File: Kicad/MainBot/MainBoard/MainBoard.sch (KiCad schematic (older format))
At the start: 20 parts, among them U1 AZ1117-3.3, U2 Teensy3.6

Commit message: update
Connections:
- net SCL1: now reaches U2.34 (37_A18_PWM_SCL1)
- net SDA1: now reaches U2.35 (38_A19_PWM_SDA1)
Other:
- note added: "Teensy/Raspeberry Pi \n comm channel\n"
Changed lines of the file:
@@
 Wire Wire Line
 	4700 4250 3900 4250
+Text Notes 750  6800 0    60   ~ 0
+Teensy/Raspeberry Pi \n    comm channel\n
+Wire Wire Line
+	4700 5050 4600 5050
+Wire Wire Line
+	4700 5150 4600 5150
+Text Label 4650 5050 2    60   ~ 0
+SCL1
+Text Label 4650 5150 2    60   ~ 0
+SDA1
 $EndSCHEMATC

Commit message: Ajout Comm Série Rasp/Teensy
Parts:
- added J?: Conn_01x02, symbol Conn_01x02
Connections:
- net RX1: now reaches J?.23 (Pin_23), U2.2 (0_RX1_MOSI1_Touch)
- net TX1: now reaches J?.22 (Pin_22), U2.3 (1_TX1_MISO1_Touch)
- new net RX_1: J?.2 (Pin_2)
- new net TX_1: J?.1 (Pin_1)
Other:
- note added: "-> RX_Pi\n-> TX_Pi"
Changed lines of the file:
@@
 Wire Wire Line
 	4700 4250 3900 4250
-Text Notes 750  6800 0    60   ~ 0
+Text Notes 500  7400 0    60   ~ 0
 Teensy/Raspeberry Pi \n    comm channel\n
 Wire Wire Line
@@
 Text Label 4650 5150 2    60   ~ 0
 SDA1
+Text Label 4150 1950 0    60   ~ 0
+TX1
+Text Label 4200 1850 0    60   ~ 0
+RX1
+$Comp
+L Conn_01x02 J?
+U 1 1 5C5C40DB
+P 1000 7550
+F 0 "J?" H 1000 7650 50  0000 C CNN
+F 1 "Conn_01x02" H 1000 7350 50  0000 C CNN
+F 2 "" H 1000 7550 50  0001 C CNN
+F 3 "" H 1000 7550 50  0001 C CNN
+	1    1000 7550
+	1    0    0    -1
+$EndComp
+Text Notes 1050 7700 0    60   ~ 0
+-> RX_Pi\n-> TX_Pi
+Wire Wire Line
+	800  7550 750  7550
+Wire Wire Line
+	800  7650 750  7650
+Text Label 750  7550 2    60   ~ 0
+TX_1
+Text Label 750  7650 2    60   ~ 0
+RX_1
 $EndSCHEMATC

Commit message: Added I2C pull-up resistor, I2C multiplexer
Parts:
- added R? (x2): R, symbol R
- added U?: TCA9548A, symbol TCA9548A
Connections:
- net GND: now also U?.~ (Vin)
- net SCL1: now also R?.1, U?.~ (Vin)
- net SDA1: now also R?.1, U?.~ (Vin)
- net VCC: now also R?.2, R?.2, U?.~ (Vin)
- net PWM17: now reaches U2.32 (35_A16_PWM)
- net PWM16: now reaches U2.33 (36_A17_PWM)
- no-connect marks 20 -> 21
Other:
- note added: "I2C Pull-up\nresistors\n"
- note added: "I2C multiplexer\n\n"
- note added: "Teensy/Raspberry Pi \n comm channel\n"
- note removed: "Teensy/Raspeberry Pi \n comm channel\n"
- moved on the sheet: J?
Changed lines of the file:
@@
 	1    0    0    -1
 $EndComp
-Wire Wire Line
-	1100 1500 1000 1500
-Wire Wire Line
-	1700 1500 1800 1500
-Wire Wire Line
-	6700 2950 6850 2950
 $Comp
 L GND #PWR?
@@
 	1    0    0    -1
 $EndComp
-Wire Wire Line
-	10300 1150 10650 1150
-Wire Wire Line
-	10300 1350 10500 1350
-Wire Wire Line
-	10500 1450 10300 1450
-Wire Wire Line
-	10300 1550 10500 1550
-Wire Wire Line
-	10500 1650 10300 1650
 NoConn ~ 10300 1750
 NoConn ~ 9350 1150
@@
 	0    -1   -1   0
 $EndComp
-Wire Wire Line
-	9350 1550 9300 1550
-Wire Wire Line
-	9350 1650 9300 1650
-Wire Wire Line
-	9350 1750 9300 1750
-Wire Wire Line
-	9350 1850 9300 1850
 Text Label 9300 1550 2    60   ~ 0
 STEP_RST_1
@@
 	0    -1   -1   0
 $EndComp
-Connection ~ 10500 1150
 $Comp
 L +12V #PWR?
@@
 NoConn ~ 9350 2550
 NoConn ~ 9350 2450
-Wire Wire Line
-	10300 2450 10500 2450
 $Comp
 L +12V #PWR?
@@
 $EndComp
 NoConn ~ 10300 3050
-Wire Wire Line
-	10300 2650 10500 2650
-Wire Wire Line
-	10500 2750 10300 2750
-Wire Wire Line
-	10300 2850 10500 2850
-Wire Wire Line
-	10500 2950 10300 2950
-Wire Wire Line
-	10300 3750 10500 3750
 $Comp
 L C C?
@@
 	1    0    0    -1
 $EndComp
-Wire Wire Line
-	10300 3950 10500 3950
-Wire Wire Line
-	10500 4050 10300 4050
-Wire Wire Line
-	10300 4150 10500 4150
-Wire Wire Line
-	10500 4250 10300 4250
 NoConn ~ 10300 4350
 $Comp
@@
 	1    0    0    -1
 $EndComp
-Wire Wire Line
-	10300 5050 10500 5050
 $Comp
 L C C?
@@
 	1    0    0    -1
 $EndComp
-Wire Wire Line
-	10300 5250 10500 5250
-Wire Wire Line
-	10500 5350 10300 5350
-Wire Wire Line
-	10300 5450 10500 5450
-Wire Wire Line
-	10500 5550 10300 5550
 NoConn ~ 10300 5650
 $Comp
@@
 Text Label 10750 6250 2    60   ~ 0
 DC_PWM_4
-Wire Wire Line
-	3900 2850 4700 2850
-Wire Wire Line
-	3900 2750 4700 2750
-Wire Wire Line
-	3900 2650 4700 2650
-Wire Wire Line
-	3900 2550 4700 2550
-Wire Wire Line
-	3900 2450 4700 2450
-Wire Wire Line
-	3900 2350 4700 2350
-Wire Wire Line
-	3900 2250 4700 2250
-Wire Wire Line
-	3900 2150 4700 2150
-Wire Wire Line
-	3900 3850 4700 3850
-Wire Wire Line
-	6700 5350 6750 5350
-Wire Wire Line
-	6700 5450 6800 5450
-Wire Wire Line
-	6700 5550 6850 5550
-Wire Wire Line
-	6700 5650 6900 5650
-Wire Wire Line
-	3900 3750 4700 3750
 $Comp
 L GND #PWR?
@@
 	0    -1   -1   0
 $EndComp
-Wire Wire Line
-	4700 1850 3900 1850
-Wire Wire Line
-	3900 1950 4700 1950
-Wire Wire Line
-	4700 2050 3900 2050
-Wire Wire Line
-	4700 2950 3900 2950
-Wire Wire Line
-	4700 3050 3900 3050
-Wire Wire Line
-	3900 3150 4700 3150
-Wire Wire Line
-	4700 3250 3900 3250
-Wire Wire Line
-	3900 3350 4700 3350
-Wire Wire Line
-	4700 3450 3900 3450
-Wire Wire Line
-	4700 3550 3900 3550
-Wire Wire Line
-	4700 3650 3900 3650
-Wire Wire Line
-	3900 3950 4700 3950
-Wire Wire Line
-	4700 4050 3900 4050
 $Comp
 L GND #PWR?
@@
 	-1   0    0    1
 $EndComp
-Wire Wire Line
-	3900 4150 4700 4150
-Wire Wire Line
-	4700 4250 3900 4250
-Text Notes 500  7400 0    60   ~ 0
-Teensy/Raspeberry Pi \n    comm channel\n
-Wire Wire Line
-	4700 5050 4600 5050
-Wire Wire Line
-	4700 5150 4600 5150
-Text Label 4650 5050 2    60   ~ 0
+Text Notes 500  7350 0    60   ~ 0
+Teensy/Raspberry Pi \n    comm channel\n
+Text Label 4350 5050 2    60   ~ 0
 SCL1
-Text Label 4650 5150 2    60   ~ 0
+Text Label 4450 5150 2    60   ~ 0
 SDA1
 Text Label 4150 1950 0    60   ~ 0
@@
 L Conn_01x02 J?
 U 1 1 5C5C40DB
-P 1000 7550
-F 0 "J?" H 1000 7650 50  0000 C CNN
-F 1 "Conn_01x02" H 1000 7350 50  0000 C CNN
-F 2 "" H 1000 7550 50  0001 C CNN
-F 3 "" H 1000 7550 50  0001 C CNN
-	1    1000 7550
-	1    0    0    -1
-$EndComp
-Text Notes 1050 7700 0    60   ~ 0
+P 1000 7500
+F 0 "J?" H 1000 7600 50  0000 C CNN
+F 1 "Conn_01x02" H 1000 7300 50  0000 C CNN
+F 2 "" H 1000 7500 50  0001 C CNN
+F 3 "" H 1000 7500 50  0001 C CNN
+	1    1000 7500
+	1    0    0    -1
+$EndComp
+Text Notes 1050 7650 0    60   ~ 0
 -> RX_Pi\n-> TX_Pi
-Wire Wire Line
-	800  7550 750  7550
-Wire Wire Line
-	800  7650 750  7650
-Text Label 750  7550 2    60   ~ 0
+Text Label 750  7500 2    60   ~ 0
 TX_1
-Text Label 750  7650 2    60   ~ 0
+Text Label 750  7600 2    60   ~ 0
 RX_1
+Text Notes 2200 6500 0    60   ~ 0
+I2C multiplexer\n\n
+$Comp
+L TCA9548A U?
+U 1 1 5C5C5BB5
+P 2700 7100
+F 0 "U?" H 2500 7750 60  0000 C CNN
+F 1 "TCA9548A" H 2700 6450 60  0000 C CNN
+F 2 "" H 2600 7150 60  0001 C CNN
+F 3 "" H 2600 7150 60  0001 C CNN
+	1    2700 7100
+	1    0    0    -1
+$EndComp
+$Comp
+L VCC #PWR?
+U 1 1 5C5C69D4
+P 2250 6550
+F 0 "#PWR?" H 2250 6400 50  0001 C CNN
+F 1 "VCC" H 2250 6700 50  0000 C CNN
+F 2 "" H 2250 6550 50  0001 C CNN
+F 3 "" H 2250 6550 50  0001 C CNN
+	1    2250 6550
+	0    -1   -1   0
+$EndComp
+$Comp
+L GND #PWR?
+U 1 1 5C5C6A14
+P 2000 6650
+F 0 "#PWR?" H 2000 6400 50  0001 C CNN
+F 1 "GND" H 2000 6500 50  0000 C CNN
+F 2 "" H 2000 6650 50  0001 C CNN
+F 3 "" H 2000 6650 50  0001 C CNN
+	1    2000 6650
+	0    1    1    0
+$EndComp
+Text Label 2200 6750 2    60   ~ 0
+SDA1
+Text Label 2200 6850 2    60   ~ 0
+SCL1
+$Comp
+L R R?
+U 1 1 5C5C7D15
+P 950 7050
+F 0 "R?" V 1030 7050 50  0000 C CNN
+F 1 "R" V 950 7050 50  0000 C CNN
+F 2 "" V 880 7050 50  0001 C CNN
+F 3 "" H 950 7050 50  0001 C CNN
+	1    950  7050
+	0    -1   -1   0
+$EndComp
+$Comp
+L R R?
+U 1 1 5C5C8548
+P 950 6850
+F 0 "R?" V 1030 6850 50  0000 C CNN
+F 1 "R" V 950 6850 50  0000 C CNN
+F 2 "" V 880 6850 50  0001 C CNN
+F 3 "" H 950 6850 50  0001 C CNN
+	1    950  6850
+	0    -1   -1   0
+$EndComp
+$Comp
+L VCC #PWR?
+U 1 1 5C5C8903
+P 1100 7050
+F 0 "#PWR?" H 1100 6900 50  0001 C CNN
+F 1 "VCC" H 1100 7200 50  0000 C CNN
+F 2 "" H 1100 7050 50  0001 C CNN
+F 3 "" H 1100 7050 50  0001 C CNN
+	1    1100 7050
+	0    1    1    0
+$EndComp
+$Comp
+L VCC #PWR?
+U 1 1 5C5C8947
+P 1100 6850
+F 0 "#PWR?" H 1100 6700 50  0001 C CNN
+F 1 "VCC" H 1100 7000 50  0000 C CNN
+F 2 "" H 1100 6850 50  0001 C CNN
+F 3 "" H 1100 6850 50  0001 C CNN
+	1    1100 6850
+	0    1    1    0
+$EndComp
+Text Label 750  7050 2    60   ~ 0
+SCL1
+Text Label 750  6850 2    60   ~ 0
+SDA1
+Text Notes 500  6750 0    60   ~ 0
+I2C Pull-up\nresistors\n
+NoConn ~ 2250 6950
+Text Label 4550 4950 2    60   ~ 0
+PWM16
+Text Label 4450 4850 2    60   ~ 0
+PWM17
+Wire Wire Line
+	1100 1500 1000 1500
+Wire Wire Line
+	1700 1500 1800 1500
+Wire Wire Line
+	6700 2950 6850 2950
+Wire Wire Line
+	10300 1150 10650 1150
+Wire Wire Line
+	10300 1350 10500 1350
+Wire Wire Line
+	10500 1450 10300 1450
+Wire Wire Line
+	10300 1550 10500 1550
+Wire Wire Line
+	10500 1650 10300 1650
+Wire Wire Line
+	9350 1550 9300 1550
+Wire Wire Line
+	9350 1650 9300 1650
+Wire Wire Line
+	9350 1750 9300 1750
+Wire Wire Line
+	9350 1850 9300 1850
+Connection ~ 10500 1150
+Wire Wire Line
+	10300 2450 10500 2450
+Wire Wire Line
+	10300 2650 10500 2650
+Wire Wire Line
+	10500 2750 10300 2750
+Wire Wire Line
+	10300 2850 10500 2850
+Wire Wire Line
+	10500 2950 10300 2950
+Wire Wire Line
+	10300 3750 10500 3750
+Wire Wire Line
+	10300 3950 10500 3950
+Wire Wire Line
+	10500 4050 10300 4050
+Wire Wire Line
+	10300 4150 10500 4150
+Wire Wire Line
+	10500 4250 10300 4250
+Wire Wire Line
+	10300 5050 10500 5050
+Wire Wire Line
+	10300 5250 10500 5250
+Wire Wire Line
+	10500 5350 10300 5350
+Wire Wire Line
+	10300 5450 10500 5450
+Wire Wire Line
+	10500 5550 10300 5550
+Wire Wire Line
+	3900 2850 4700 2850
+Wire Wire Line
+	3900 2750 4700 2750
+Wire Wire Line
+	3900 2650 4700 2650
+Wire Wire Line
+	3900 2550 4700 2550
+Wire Wire Line
+	3900 2450 4700 2450
+Wire Wire Line
+	3900 2350 4700 2350
+Wire Wire Line
+	3900 2250 4700 2250
+Wire Wire Line
+	3900 2150 4700 2150
+Wire Wire Line
+	3900 3850 4700 3850
+Wire Wire Line
+	6700 5350 6750 5350
+Wire Wire Line
+	6700 5450 6800 5450
+Wire Wire Line
+	6700 5550 6850 5550
+Wire Wire Line
+	6700 5650 6900 5650
+Wire Wire Line
+	3900 3750 4700 3750
+Wire Wire Line
+	4700 1850 3900 1850
+Wire Wire Line
+	3900 1950 4700 1950
+Wire Wire Line
+	4700 2050 3900 2050
+Wire Wire Line
+	4700 2950 3900 2950
+Wire Wire Line
+	4700 3050 3900 3050
+Wire Wire Line
+	3900 3150 4700 3150
+Wire Wire Line
+	4700 3250 3900 3250
+Wire Wire Line
+	3900 3350 4700 3350
+Wire Wire Line
+	4700 3450 3900 3450
+Wire Wire Line
+	4700 3550 3900 3550
+Wire Wire Line
+	4700 3650 3900 3650
+Wire Wire Line
+	3900 3950 4700 3950
+Wire Wire Line
+	4700 4050 3900 4050
+Wire Wire Line
+	3900 4150 4700 4150
+Wire Wire Line
+	4700 4250 3900 4250
+Wire Wire Line
+	4350 5050 4700 5050
+Wire Wire Line
+	4450 5150 4700 5150
+Wire Wire Line
+	800  7500 750  7500
+Wire Wire Line
+	800  7600 750  7600
+Wire Wire Line
+	2000 6650 2250 6650
+Wire Wire Line
+	2250 6750 2200 6750
+Wire Wire Line
+	2250 6850 2200 6850
+Wire Wire Line
+	800  7050 750  7050
+Wire Wire Line
+	750  6850 800  6850
+Wire Notes Line
+	500  7150 1500 7150
+Wire Notes Line
+	1300 7150 1300 6550
+Wire Notes Line
+	1300 6550 500  6550
+Wire Notes Line
+	500  6550 500  7750
+Wire Notes Line
+	500  7750 1500 7750
+Wire Notes Line
+	1500 7750 1500 7150
+Wire Wire Line
+	4700 4950 4550 4950
+Wire Wire Line
+	4700 4850 4450 4850
 $EndSCHEMATC

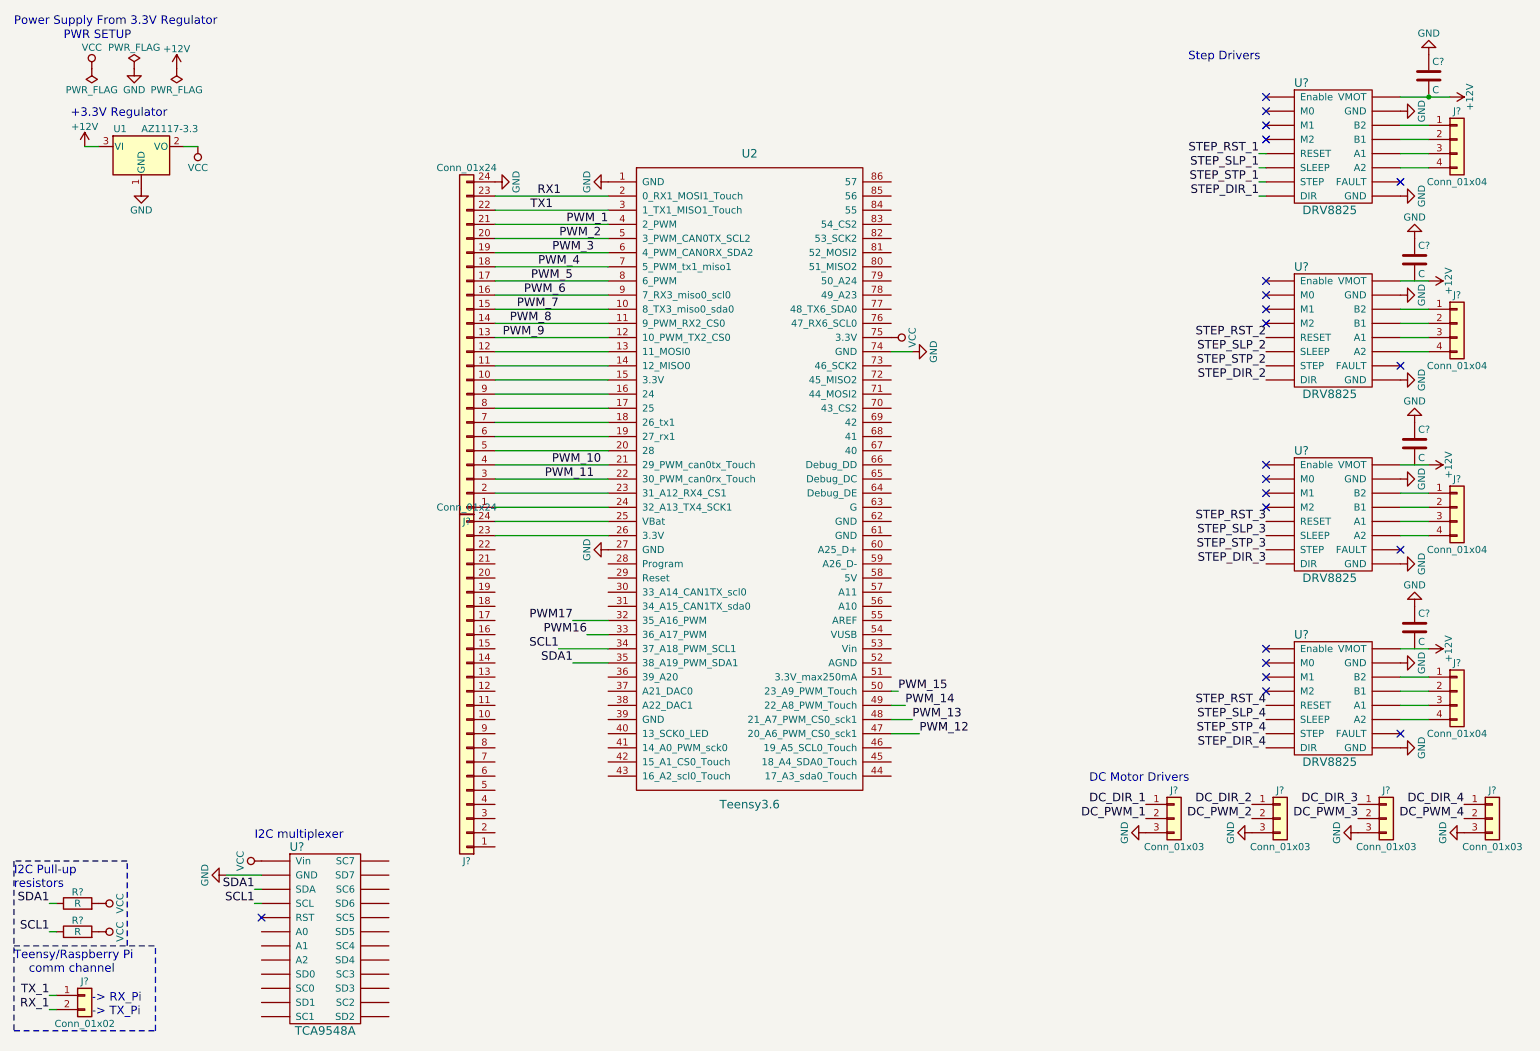
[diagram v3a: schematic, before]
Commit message: Finished female headers
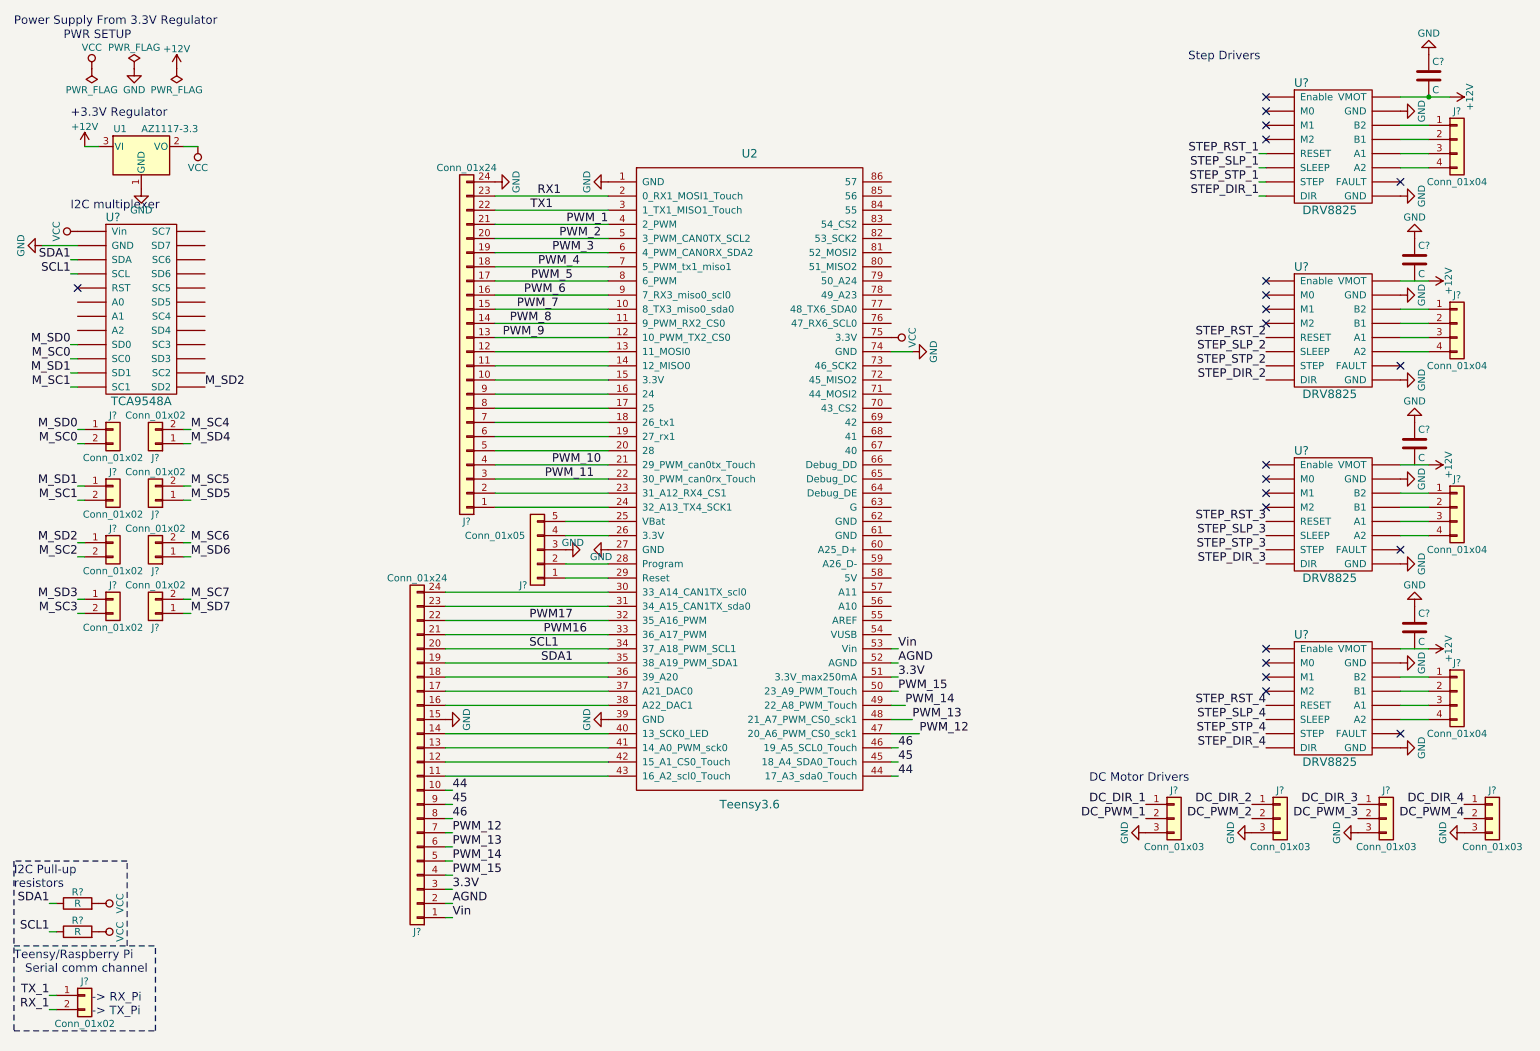
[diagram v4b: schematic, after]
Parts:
- removed J?: Conn_01x24, symbol Conn_01x24
- added J? (x8): Conn_01x02, symbol Conn_01x02
- added J?: Conn_01x24, symbol Conn_01x24
- added J?: Conn_01x05, symbol Conn_01x05
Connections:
- net GND: now also U2.39 (GND), J?.15 (Pin_15), J?.3 (Pin_3)
- net PWM16: now also J?.21 (Pin_21)
- net PWM17: now also J?.22 (Pin_22)
- net PWM_12: now also J?.7 (Pin_7)
- net PWM_13: now also J?.6 (Pin_6)
- net PWM_14: now also J?.5 (Pin_5)
- net PWM_15: now also J?.4 (Pin_4)
- net SCL1: now also J?.20 (Pin_20)
- net SDA1: now also J?.19 (Pin_19)
- net at U2.25 (VBat): now also J?.5 (Pin_5)
- net at U2.26 (3.3V): now also J?.4 (Pin_4)
- net at U2.28 (Program): now also J?.2 (Pin_2)
- net at U2.29 (Reset): now also J?.1 (Pin_1)
- net at U2.30 (33_A14_CAN1TX_scl0): now also J?.24 (Pin_24)
- net at U2.31 (34_A15_CAN1TX_sda0): now also J?.23 (Pin_23)
- net at U2.36 (39_A20): now also J?.18 (Pin_18)
- net at U2.37 (A21_DAC0): now also J?.17 (Pin_17)
- net at U2.38 (A22_DAC1): now also J?.16 (Pin_16)
- net at U2.40 (13_SCK0_LED): now also J?.14 (Pin_14)
- net at U2.41 (14_A0_PWM_sck0): now also J?.13 (Pin_13)
- net at U2.42 (15_A1_CS0_Touch): now also J?.12 (Pin_12)
- net at U2.43 (16_A2_scl0_Touch): now also J?.11 (Pin_11)
- net 44: now reaches U2.44 (17_A3_sda0_Touch)
- net 44: now also J?.10 (Pin_10)
- net 45: now reaches U2.45 (18_A4_SDA0_Touch)
- net 45: now also J?.9 (Pin_9)
- net 46: now reaches U2.46 (19_A5_SCL0_Touch)
- net 46: now also J?.8 (Pin_8)
- net 3.3V: now reaches U2.51 (3.3V_max250mA)
- net 3.3V: now also J?.3 (Pin_3)
- net AGND: now reaches U2.52 (AGND)
- net AGND: now also J?.2 (Pin_2)
- net Vin: now reaches U2.53 (Vin)
- net Vin: now also J?.1 (Pin_1)
- new net M_SC0: J?.2 (Pin_2), U?.~ (Vin)
- new net M_SC1: J?.2 (Pin_2), U?.~ (Vin)
- new net M_SC2: J?.2 (Pin_2)
- new net M_SC3: J?.2 (Pin_2)
- new net M_SC4: J?.2 (Pin_2)
- new net M_SC5: J?.2 (Pin_2)
- new net M_SC6: J?.2 (Pin_2)
- new net M_SC7: J?.2 (Pin_2)
- new net M_SD0: J?.1 (Pin_1), U?.~ (Vin)
- new net M_SD1: J?.1 (Pin_1), U?.~ (Vin)
- new net M_SD2: J?.1 (Pin_1), U?.~ (Vin)
- new net M_SD3: J?.1 (Pin_1)
- new net M_SD4: J?.1 (Pin_1)
- new net M_SD5: J?.1 (Pin_1)
- new net M_SD6: J?.1 (Pin_1)
- new net M_SD7: J?.1 (Pin_1)
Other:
- note added: "Teensy/Raspberry Pi \n Serial comm channel\n"
- note removed: "Teensy/Raspberry Pi \n comm channel\n"
- moved on the sheet: U?
